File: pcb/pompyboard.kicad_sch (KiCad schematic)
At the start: 16 parts, among them J1 USB_C_Receptacle_USB2.0_16P, J2 Conn_01x04_Pin, SW1 EVQQ2B03W, U229 STM32F429IGT6, U231 TPS62152

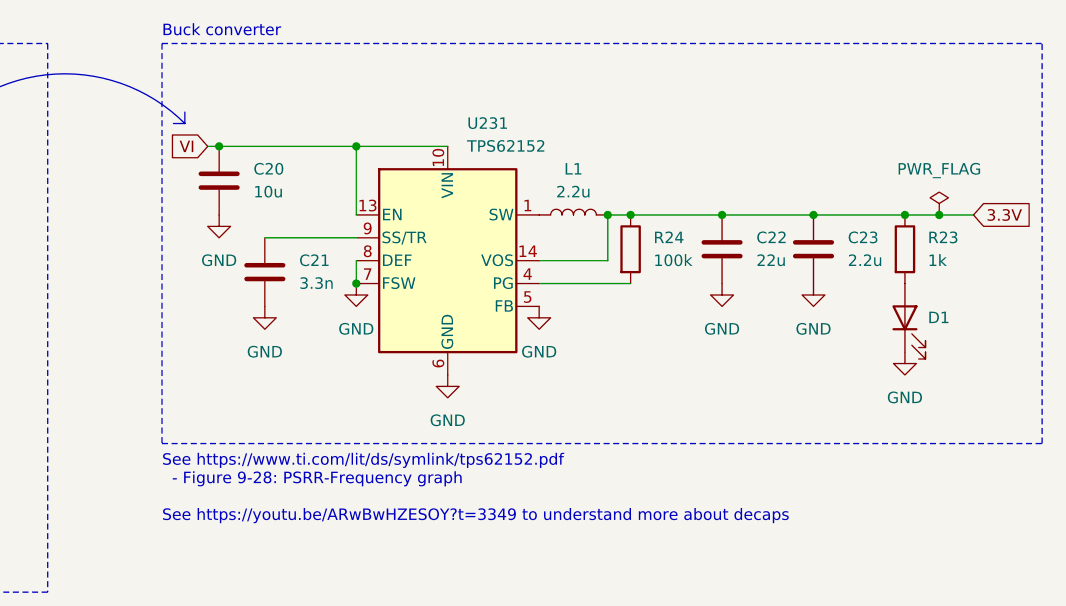
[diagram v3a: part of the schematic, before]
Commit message: pcb: remove decap that's too small for economic plan
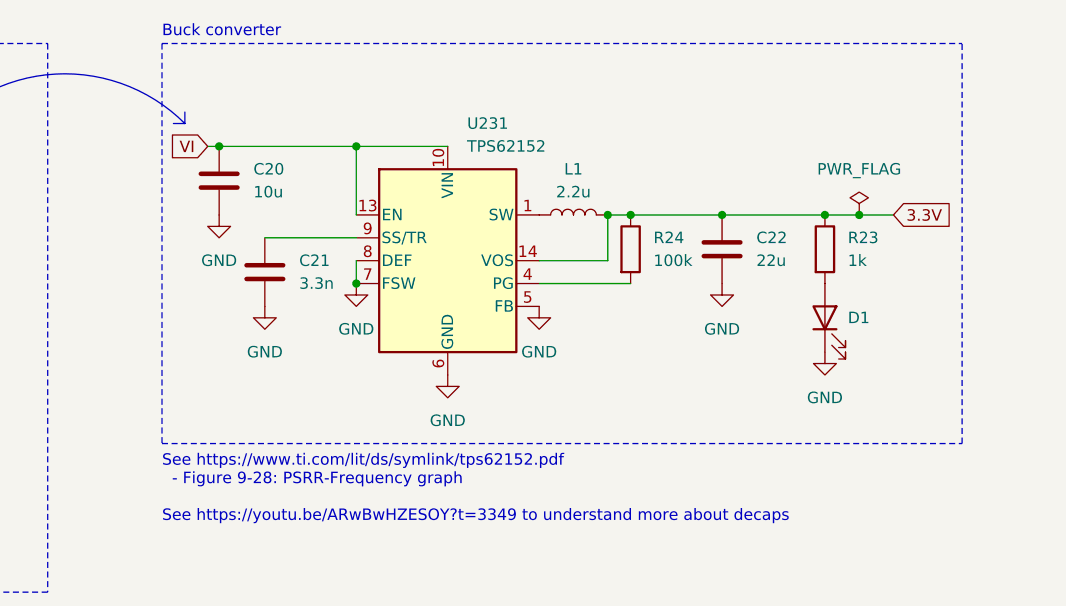
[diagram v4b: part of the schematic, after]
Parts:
- removed C23: 2.2u, Capacitor_SMD:C_0201_0603Metric, symbol Device:C
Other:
- moved on the sheet: D1, R23
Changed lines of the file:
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@@
 	)
 	(junction
-		(at 327.66 44.45)
+		(at 318.77 44.45)
 		(diameter 0)
 		(color 0 0 0 0)
@@
 	)
 	(junction
-		(at 331.47 44.45)
+		(at 322.58 44.45)
 		(diameter 0)
 		(color 0 0 0 0)
@@
 	)
 	(junction
-		(at 317.5 44.45)
-		(diameter 0)
-		(color 0 0 0 0)
-	)
-	(junction
 		(at 71.12 34.29)
 		(diameter 0)
@@
 	(polyline
 		(pts
-			(xy 342.9 69.85) (xy 342.9 25.4)
+			(xy 334.01 69.85) (xy 334.01 25.4)
 		)
 		(stroke
@@
 	(wire
 		(pts
-			(xy 331.47 44.45) (xy 335.28 44.45)
+			(xy 322.58 44.45) (xy 326.39 44.45)
 		)
 		(stroke
@@
 	(polyline
 		(pts
-			(xy 245.11 69.85) (xy 342.9 69.85)
+			(xy 245.11 69.85) (xy 334.01 69.85)
 		)
 		(stroke
@@
 	(polyline
 		(pts
-			(xy 245.11 25.4) (xy 342.9 25.4)
+			(xy 245.11 25.4) (xy 334.01 25.4)
 		)
 		(stroke
@@
 	(wire
 		(pts
-			(xy 307.34 44.45) (xy 317.5 44.45)
+			(xy 307.34 44.45) (xy 318.77 44.45)
 		)
 		(stroke
@@
 	(wire
 		(pts
-			(xy 327.66 44.45) (xy 331.47 44.45)
+			(xy 318.77 44.45) (xy 322.58 44.45)
 		)
 		(stroke
@@
 	(wire
 		(pts
-			(xy 317.5 44.45) (xy 327.66 44.45)
-		)
-		(stroke
-			(width 0)
-			(type default)
-		)
-	)
-	(wire
-		(pts
 			(xy 83.82 34.29) (xy 86.36 34.29)
 		)
@@
 	(global_label "3.3V"
 		(shape input)
-		(at 335.28 44.45 0)
+		(at 326.39 44.45 0)
 		(fields_autoplaced yes)
 		(effects
@@
 		)
 		(property "Intersheetrefs" "${INTERSHEET_REFS}"
-			(at 342.3776 44.45 0)
+			(at 333.4876 44.45 0)
 			(effects
 				(font
@@
 	)
 	(symbol
-		(lib_id "power:GND")
-		(at 317.5 52.07 0)
-		(unit 1)
-		(exclude_from_sim no)
-		(in_bom yes)
-		(on_board yes)
-		(dnp no)
-		(fields_autoplaced yes)
-		(property "Reference" "#PWR056"
-			(at 317.5 58.42 0)
-			(effects
-				(font
-					(size 1.27 1.27)
-				)
-				(hide yes)
-			)
-		)
-		(property "Value" "GND"
-			(at 317.5 57.15 0)
-			(effects
-				(font
-					(size 1.27 1.27)
-				)
-			)
-		)
-		(property "Footprint" ""
-			(at 317.5 52.07 0)
-			(effects
-				(font
-					(size 1.27 1.27)
-				)
-				(hide yes)
-			)
-		)
-		(property "Datasheet" ""
-			(at 317.5 52.07 0)
-			(effects
-				(font
-					(size 1.27 1.27)
-				)
-				(hide yes)
-			)
-		)
-		(property "Description" "Power symbol creates a global label with name \"GND\" , ground"
-			(at 317.5 52.07 0)
-			(effects
-				(font
-					(size 1.27 1.27)
-				)
-				(hide yes)
-			)
-		)
-		(pin "1"
-		)
-		(instances
-			(project "pompyboard"
-				(path "/e5830f2e-b6bc-440e-bdf9-7651ab21e3a0"
-					(reference "#PWR056")
-					(unit 1)
-				)
-			)
-		)
-	)
-	(symbol
 		(lib_id "Device:R")
-		(at 327.66 48.26 0)
+		(at 318.77 48.26 0)
 		(unit 1)
 		(exclude_from_sim no)
@@
 		(fields_autoplaced yes)
 		(property "Reference" "R23"
-			(at 330.2 46.9899 0)
+			(at 321.31 46.9899 0)
 			(effects
 				(font
@@
 		)
 		(property "Value" "1k"
-			(at 330.2 49.5299 0)
+			(at 321.31 49.5299 0)
 			(effects
 				(font
@@
 		)
 		(property "Footprint" "Resistor_SMD:R_0402_1005Metric"
-			(at 325.882 48.26 90)
+			(at 316.992 48.26 90)
 			(effects
 				(font
@@
 		)
 		(property "Datasheet" "~"
-			(at 327.66 48.26 0)
+			(at 318.77 48.26 0)
 			(effects
 				(font
@@
 		)
 		(property "Description" "Resistor"
-			(at 327.66 48.26 0)
+			(at 318.77 48.26 0)
 			(effects
 				(font
@@
 		)
 		(property "LCSC Part #" "C11702"
-			(at 327.66 48.26 0)
+			(at 318.77 48.26 0)
 			(effects
 				(font
@@
 	(symbol
 		(lib_id "Device:LED")
-		(at 327.66 55.88 90)
+		(at 318.77 55.88 90)
 		(unit 1)
 		(exclude_from_sim no)
@@
 		(dnp no)
 		(property "Reference" "D1"
-			(at 330.2 55.88 90)
+			(at 321.31 55.88 90)
 			(effects
 				(font
@@
 		)
 		(property "Value" "F.0603.00139/P2-0603R1TS2-06T-002"
-			(at 331.47 58.7374 90)
+			(at 322.58 58.7374 90)
 			(effects
 				(font
@@
 		)
 		(property "Footprint" "LED_SMD:LED_0603_1608Metric"
-			(at 327.66 55.88 0)
+			(at 318.77 55.88 0)
 			(effects
 				(font
@@
 		)
 		(property "Datasheet" "https://jlcpcb.com/api/file/downloadByFileSystemAccessId/8590909078942269440"
-			(at 327.66 55.88 0)
+			(at 318.77 55.88 0)
 			(effects
 				(font
@@
 		)
 		(property "Description" "Light emitting diode"
-			(at 327.66 55.88 0)
+			(at 318.77 55.88 0)
 			(effects
 				(font
@@
 		)
 		(property "Sim.Pins" "1=K 2=A"
-			(at 327.66 55.88 0)
+			(at 318.77 55.88 0)
 			(effects
 				(font
@@
 		)
 		(property "LCSC Part #" "C7496820"
-			(at 327.66 55.88 90)
+			(at 318.77 55.88 90)
 			(effects
 				(font
@@
 	(symbol
 		(lib_id "power:PWR_FLAG")
-		(at 331.47 44.45 0)
+		(at 322.58 44.45 0)
 		(unit 1)
 		(exclude_from_sim no)
@@
 		(fields_autoplaced yes)
 		(property "Reference" "#FLG02"
-			(at 331.47 42.545 0)
+			(at 322.58 42.545 0)
 			(effects
 				(font
@@
 		)
 		(property "Value" "PWR_FLAG"
-			(at 331.47 39.37 0)
+			(at 322.58 39.37 0)
 			(effects
 				(font
@@
 		)
 		(property "Footprint" ""
-			(at 331.47 44.45 0)
+			(at 322.58 44.45 0)
 			(effects
 				(font
@@
 		)
 		(property "Datasheet" "~"
-			(at 331.47 44.45 0)
+			(at 322.58 44.45 0)
 			(effects
 				(font
@@
 		)
 		(property "Description" "Special symbol for telling ERC where power comes from"
-			(at 331.47 44.45 0)
+			(at 322.58 44.45 0)
 			(effects
 				(font
@@
 	)
 	(symbol
-		(lib_id "Device:C")
-		(at 317.5 48.26 0)
-		(unit 1)
-		(exclude_from_sim no)
-		(in_bom yes)
-		(on_board yes)
-		(dnp no)
-		(property "Reference" "C23"
-			(at 321.31 46.9899 0)
-			(effects
-				(font
-					(size 1.27 1.27)
-				)
-				(justify left)
-			)
-		)
-		(property "Value" "2.2u"
-			(at 321.31 49.5299 0)
-			(effects
-				(font
-					(size 1.27 1.27)
-				)
-				(justify left)
-			)
-		)
-		(property "Footprint" "Capacitor_SMD:C_0201_0603Metric"
-			(at 318.4652 52.07 0)
-			(effects
-				(font
-					(size 1.27 1.27)
-				)
-				(hide yes)
-			)
-		)
-		(property "Datasheet" "~"
-			(at 317.5 48.26 0)
-			(effects
-				(font
-					(size 1.27 1.27)
-				)
-				(hide yes)
-			)
-		)
-		(property "Description" "Unpolarized capacitor"
-			(at 317.5 48.26 0)
-			(effects
-				(font
-					(size 1.27 1.27)
-				)
-				(hide yes)
-			)
-		)
-		(property "LCSC Part #" "C335106"
-			(at 317.5 48.26 0)
-			(effects
-				(font
-					(size 1.27 1.27)
-				)
-				(hide yes)
-			)
-		)
-		(pin "2"
-		)
-		(pin "1"
-		)
-		(instances
-			(project "pompyboard"
-				(path "/e5830f2e-b6bc-440e-bdf9-7651ab21e3a0"
-					(reference "C23")
-					(unit 1)
-				)
-			)
-		)
-	)
-	(symbol
 		(lib_id "power:GND")
-		(at 327.66 59.69 0)
+		(at 318.77 59.69 0)
 		(unit 1)
 		(exclude_from_sim no)
@@
 		(fields_autoplaced yes)
 		(property "Reference" "#PWR0487"
-			(at 327.66 66.04 0)
+			(at 318.77 66.04 0)
 			(effects
 				(font
@@
 		)
 		(property "Value" "GND"
-			(at 327.66 64.77 0)
+			(at 318.77 64.77 0)
 			(effects
 				(font
@@
 		)
 		(property "Footprint" ""
-			(at 327.66 59.69 0)
+			(at 318.77 59.69 0)
 			(effects
 				(font
@@
 		)
 		(property "Datasheet" ""
-			(at 327.66 59.69 0)
+			(at 318.77 59.69 0)
 			(effects
 				(font
@@
 		)
 		(property "Description" "Power symbol creates a global label with name \"GND\" , ground"
-			(at 327.66 59.69 0)
+			(at 318.77 59.69 0)
 			(effects
 				(font

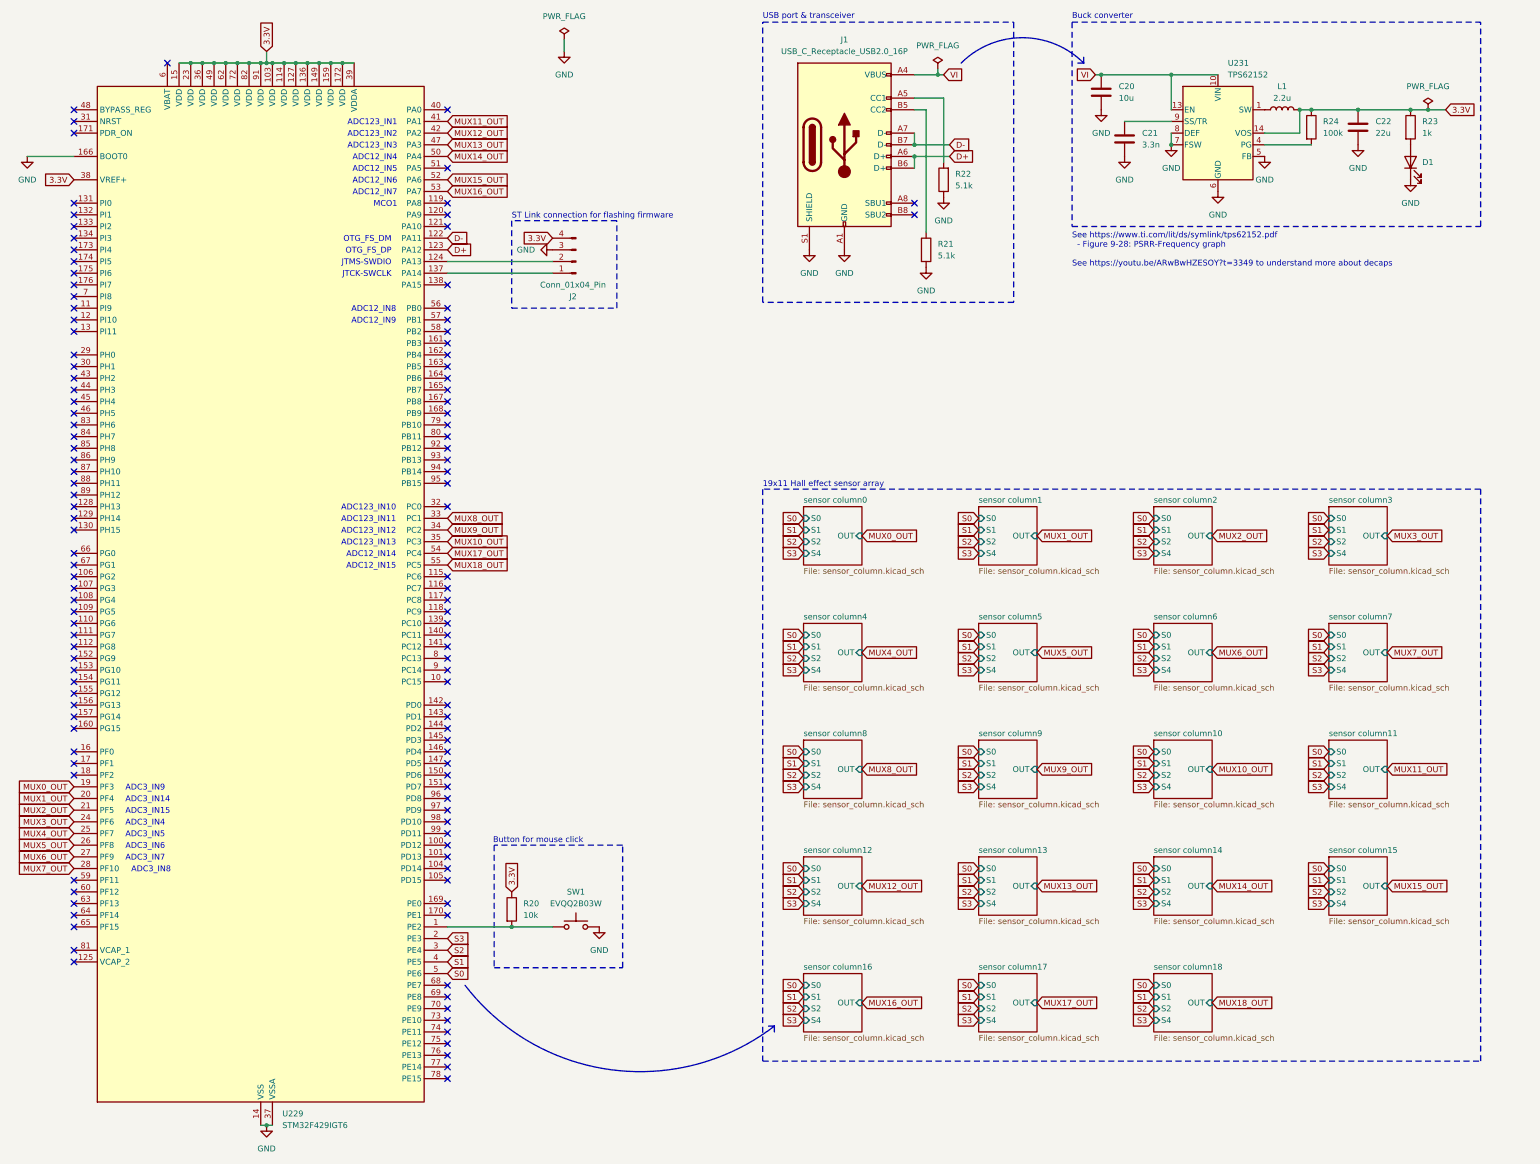
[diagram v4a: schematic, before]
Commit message: pcb: add 1 more button for a total of 2
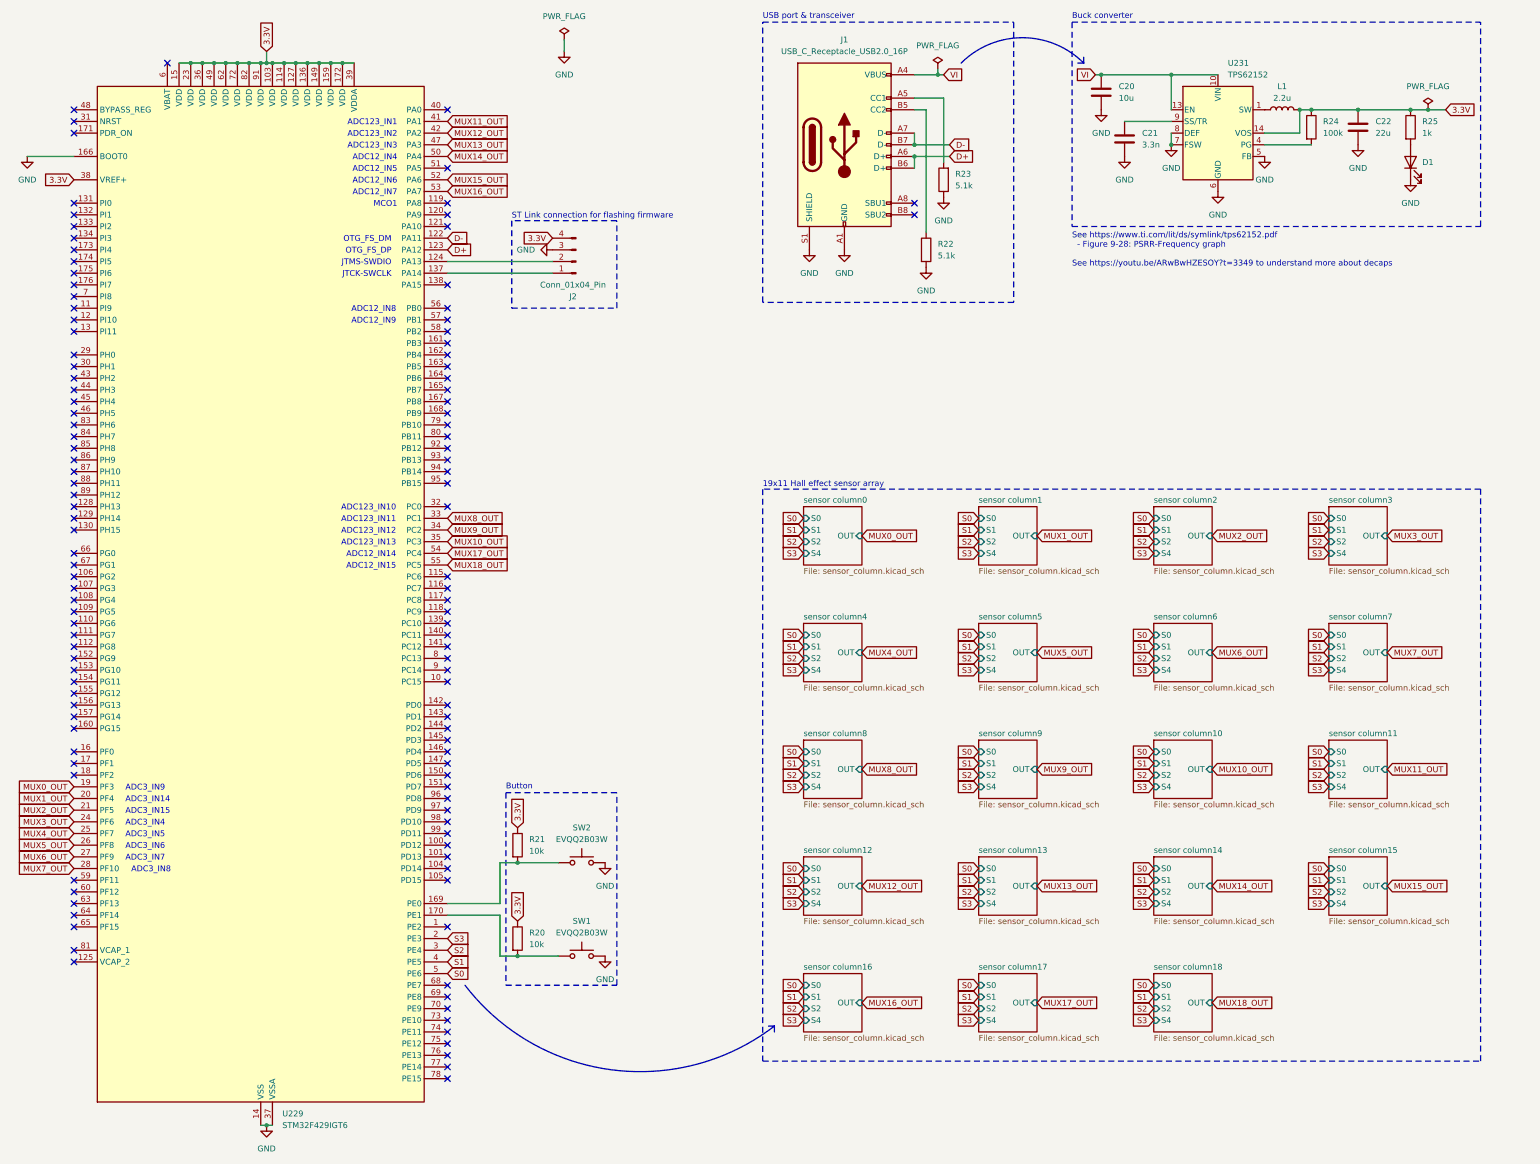
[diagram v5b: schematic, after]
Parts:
- added R21: 10k, Resistor_SMD:R_0402_1005Metric, symbol Device:R
- added SW2: EVQQ2B03W, Button_Switch_SMD:SW_SPST_EVQQ2, symbol Switch:SW_Push
- renumbered R21 to R22, R22 to R23, R23 to R25
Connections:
- net 3.3V: now also R21.1
- net GND: now also SW2.2
- net at R20.2, SW1.1: now also U229.170 (PE1); no longer U229.1 (PE2)
- net at U229.169 (PE0): now also R21.2, SW2.1
- no-connect marks 120 -> 119
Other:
- note added: "Button"
- note removed: "Button for mouse click"
- moved on the sheet: R20, SW1
